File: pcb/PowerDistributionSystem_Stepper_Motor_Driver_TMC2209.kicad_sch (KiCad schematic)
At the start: 19 parts, among them U1 TMC2209-LA-T

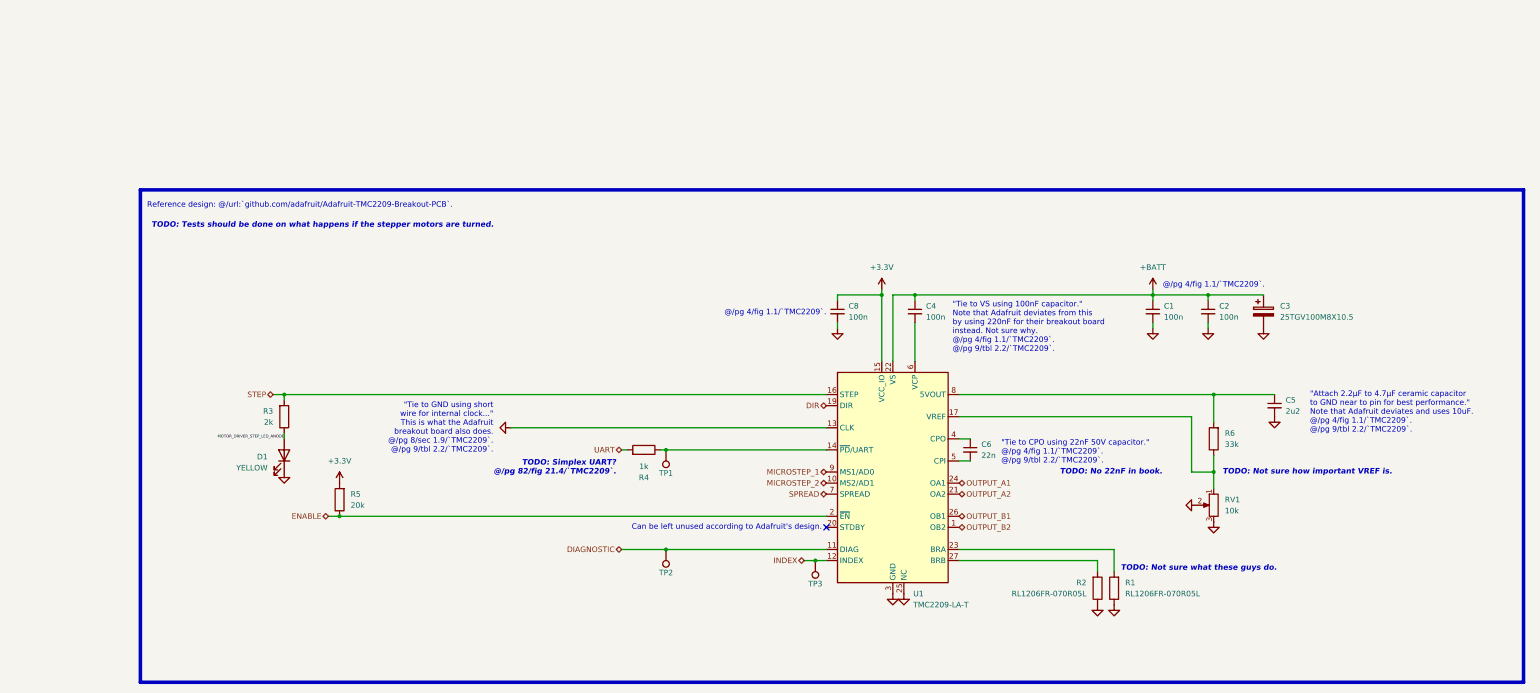
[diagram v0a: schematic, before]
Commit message: Cleaned up small details of the TMC2209.
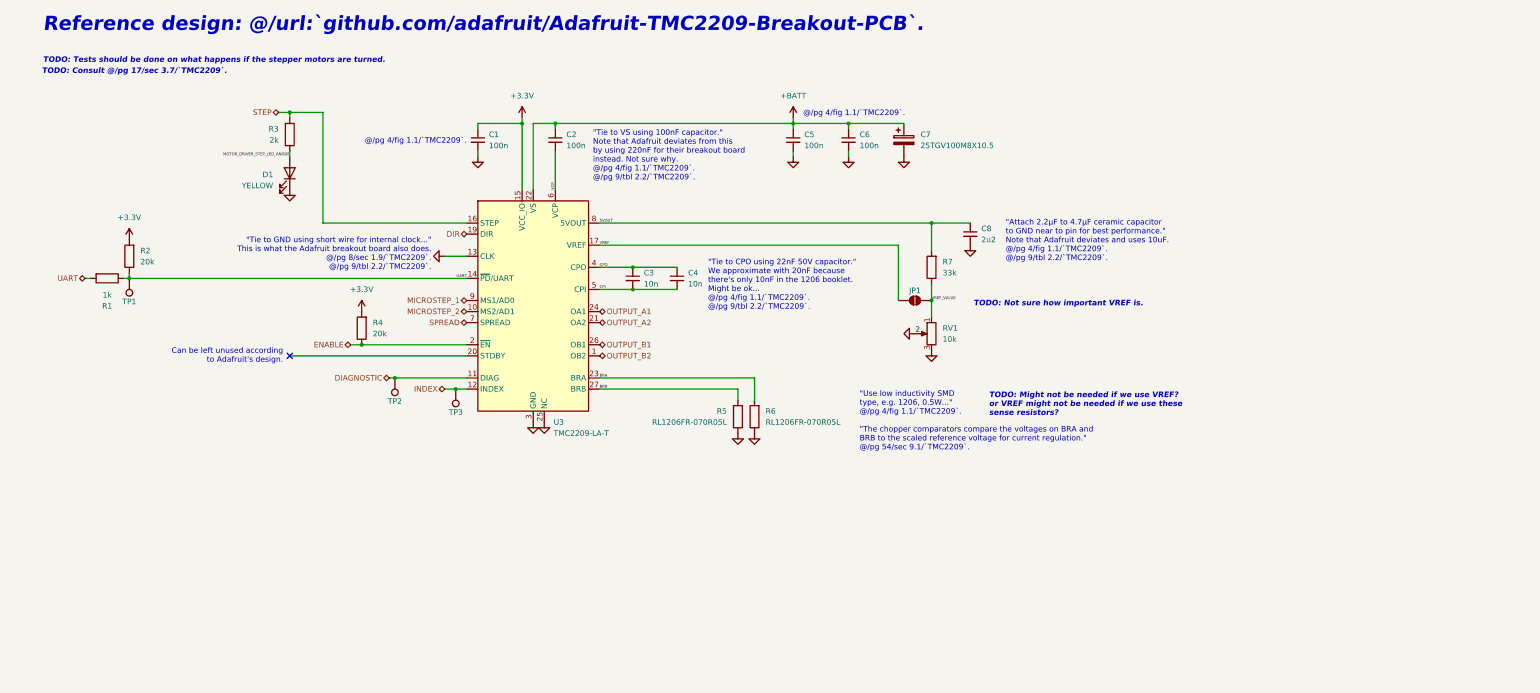
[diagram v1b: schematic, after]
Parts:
- added C4: 10n, Capacitor_SMD:C_1206_3216Metric_Pad1.33x1.80mm_HandSolder, symbol Device:C_Small
- added JP1: SolderJumper_2_Open, symbol Jumper:SolderJumper_2_Open
- added R2: 20k, Resistor_SMD:R_1206_3216Metric_Pad1.30x1.75mm_HandSolder, symbol Device:R
- C3: renamed from C6; value 22n -> 10n
- renumbered C8 to C1, C4 to C2, C1 to C5, C2 to C6, C3 to C7, C5 to C8, R4 to R1, R5 to R4, R2 to R5, R1 to R6, R6 to R7, U1 to U3
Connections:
- net +3.3V: now also R2.2
- net UART: now also R1.1, TP1.1, U3.14 (~{PD}/UART), R2.1
- net CPO: now reaches C3.1, U3.4 (CPO)
- net CPO: now also C4.1
- net CPI: now reaches C3.2, U3.5 (CPI)
- net CPI: now also C4.2
- net BRB: now reaches R5.2, U3.27 (BRB)
- net VREF_VALUE: now reaches R7.1, RV1.1
- net VREF_VALUE: now also JP1.2 (B); no longer U3.17 (VREF)
- net 5VOUT: now reaches C8.1, R7.2, U3.8 (5VOUT)
- net BRA: now reaches R6.2, U3.23 (BRA)
- net VCP: now reaches C2.2, U3.6 (VCP)
- new net VREF: JP1.1 (A), U3.17 (VREF)
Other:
- note added: ""Tie to CPO using 22nF 50V capacitor." We approximate with 20nF because there's only 10nF in the 1206 booklet. Might be ok... @/pg 4/fig 1.1/`TMC2209`. @/pg 9/tbl 2.2/`TMC2209`."
- note added: ""Use low inductivity SMD type, e.g. 1206, 0.5W..." @/pg 4/fig 1.1/`TMC2209`. "The chopper comparators compare the voltages on BRA and BRB to the scaled reference voltage for current regulation." @/pg 54/sec 9.1/`TMC2209`."
- note added: "TODO: Consult @/pg 17/sec 3.7/`TMC2209`."
- note added: "TODO: Might not be needed if we use VREF? or VREF might not be needed if we use these sense resistors?"
- note removed: ""Tie to CPO using 22nF 50V capacitor." @/pg 4/fig 1.1/`TMC2209`. @/pg 9/tbl 2.2/`TMC2209`."
- note removed: "TODO: No 22nF in book."
- note removed: "TODO: Not sure what these guys do."
- note removed: "TODO: Simplex UART? @/pg 82/fig 21.4/`TMC2209`."
- moved on the sheet: C1, C2, C3, C5, C6, C7, C8, D1, R1, R3, R4, R5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

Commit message: Reworked TMC2209 so that the three drivers have things in common (e.g. enable/disable pin).
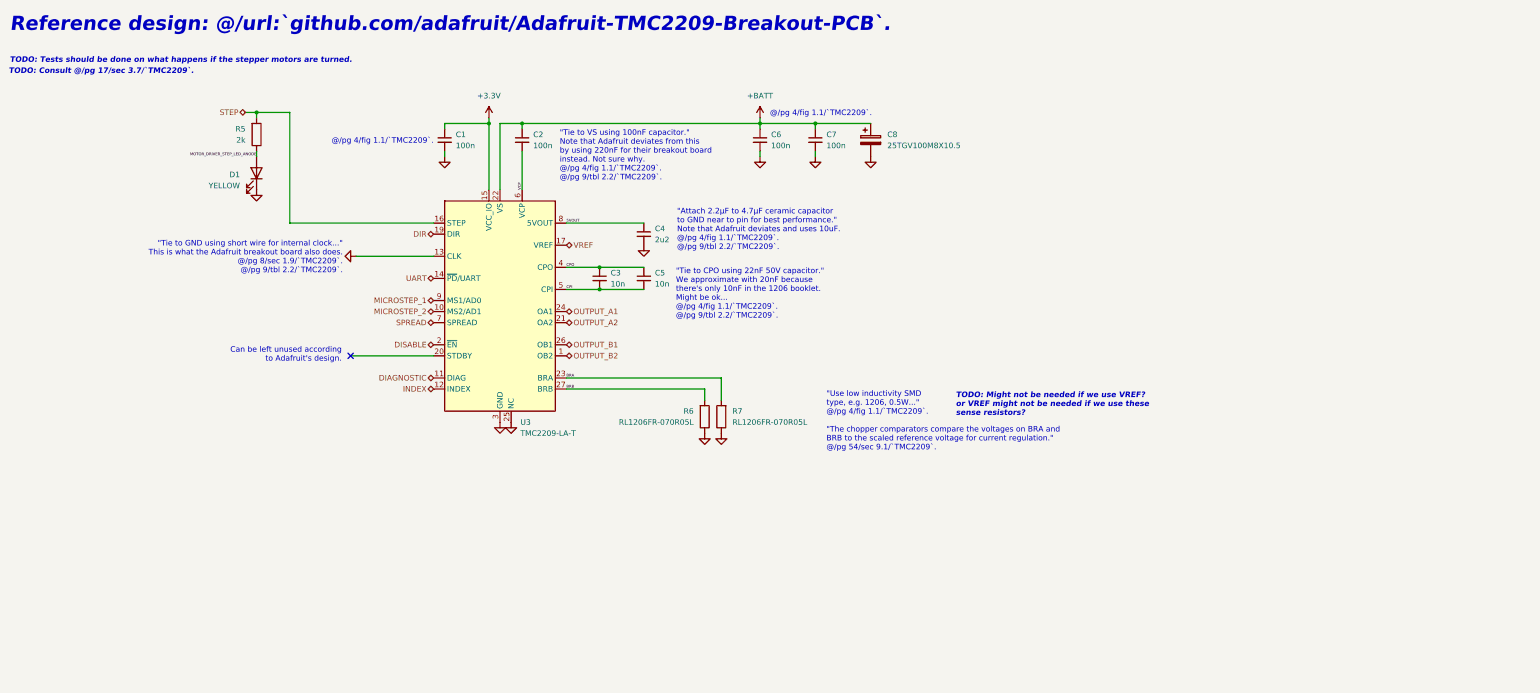
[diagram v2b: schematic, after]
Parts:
- removed JP1: SolderJumper_2_Open, symbol Jumper:SolderJumper_2_Open
- removed R1: 1k, Resistor_SMD:R_1206_3216Metric_Pad1.30x1.75mm_HandSolder, symbol Device:R
- removed R2, R4: 20k, Resistor_SMD:R_1206_3216Metric_Pad1.30x1.75mm_HandSolder, symbol Device:R
- removed R7: 33k, Resistor_SMD:R_1206_3216Metric_Pad1.30x1.75mm_HandSolder, symbol Device:R
- removed RV1: 10k, pcb:TRIM_35WR10KLFTR, symbol Device:R_Potentiometer
- removed TP1, TP2, TP3: TestPoint, TestPoint:TestPoint_Pad_1.0x1.0mm, symbol Connector:TestPoint
- renumbered C8 to C4, C4 to C5, C5 to C6, C6 to C7, C7 to C8, R3 to R5, R5 to R6, R6 to R7
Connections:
- net ENABLE renamed DISABLE
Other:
- note removed: "TODO: Not sure how important VREF is."
- moved on the sheet: C1, C2, C3, C4, C5, C6, C7, C8, D1, R5, R6, R7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

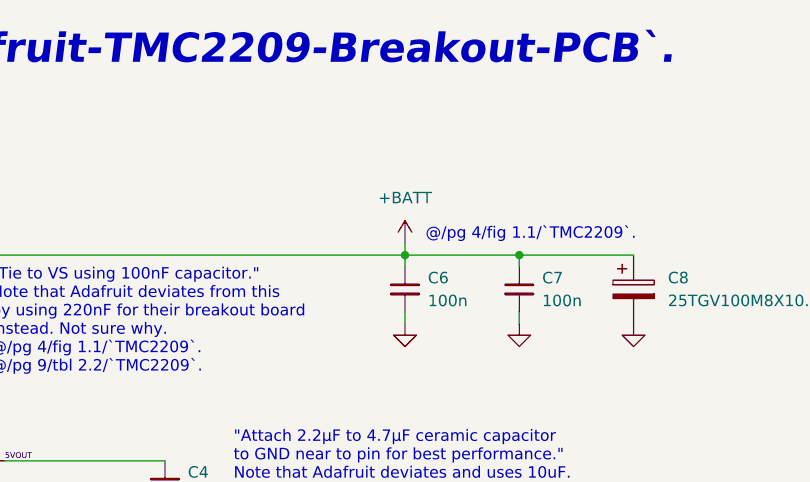
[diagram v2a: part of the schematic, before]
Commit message: Added load switch.
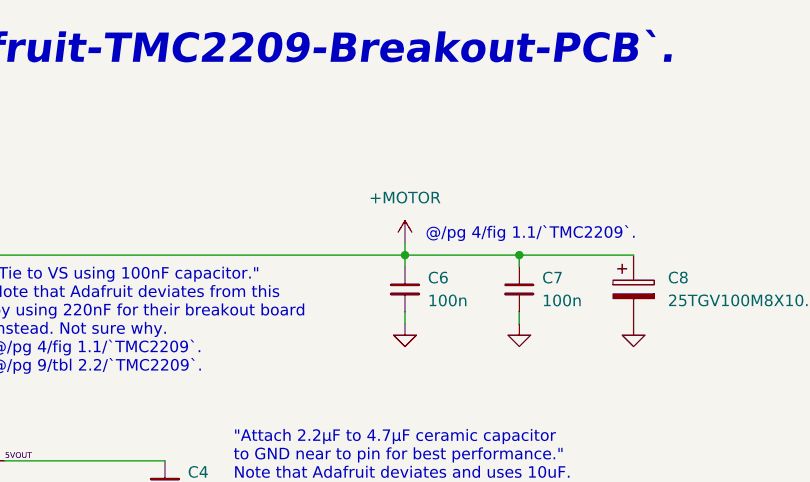
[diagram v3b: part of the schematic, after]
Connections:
- net +BATT renamed +MOTOR
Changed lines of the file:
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@@
 			)
 		)
-		(property "Value" "+BATT"
+		(property "Value" "+MOTOR"
 			(at 189.23 73.66 0)
 			(effects

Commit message: Fixed footprint of TMC2209-LA-T.
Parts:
- U3: footprint Package_DFN_QFN:VQFN-28-1EP_5x5mm_P0.5mm_EP3.7x3.7mm_ThermalVias -> pcb:VQFN-28-1EP_5x5mm_P0.5mm_EP3.7x3.7mm_ThermalVias
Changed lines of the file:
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@@
 			)
 		)
-		(property "Footprint" "Package_DFN_QFN:VQFN-28-1EP_5x5mm_P0.5mm_EP3.7x3.7mm_ThermalVias"
+		(property "Footprint" "pcb:VQFN-28-1EP_5x5mm_P0.5mm_EP3.7x3.7mm_ThermalVias"
 			(at 129.54 151.13 0)
 			(effects

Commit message: Updated power distribution system with new stack-up layout.
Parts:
- U3: footprint pcb:VQFN-28-1EP_5x5mm_P0.5mm_EP3.7x3.7mm_ThermalVias -> Package_DFN_QFN:VQFN-28-1EP_5x5mm_P0.5mm_EP3.7x3.7mm_ThermalVias
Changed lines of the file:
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@@
 			)
 		)
-		(property "Footprint" "pcb:VQFN-28-1EP_5x5mm_P0.5mm_EP3.7x3.7mm_ThermalVias"
+		(property "Footprint" "Package_DFN_QFN:VQFN-28-1EP_5x5mm_P0.5mm_EP3.7x3.7mm_ThermalVias"
 			(at 129.54 151.13 0)
 			(effects

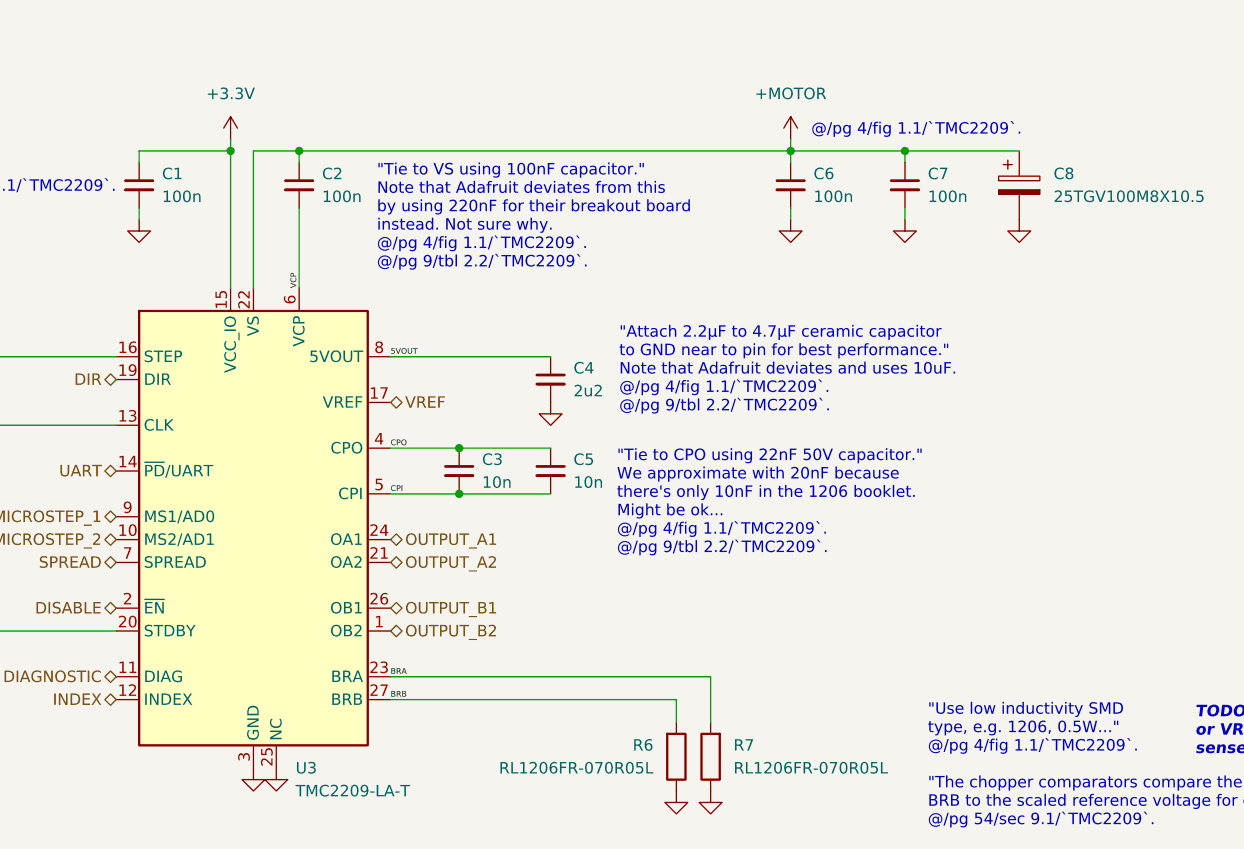
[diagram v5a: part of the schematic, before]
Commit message: Updated `StackConnector` to use reference prefix of "J".
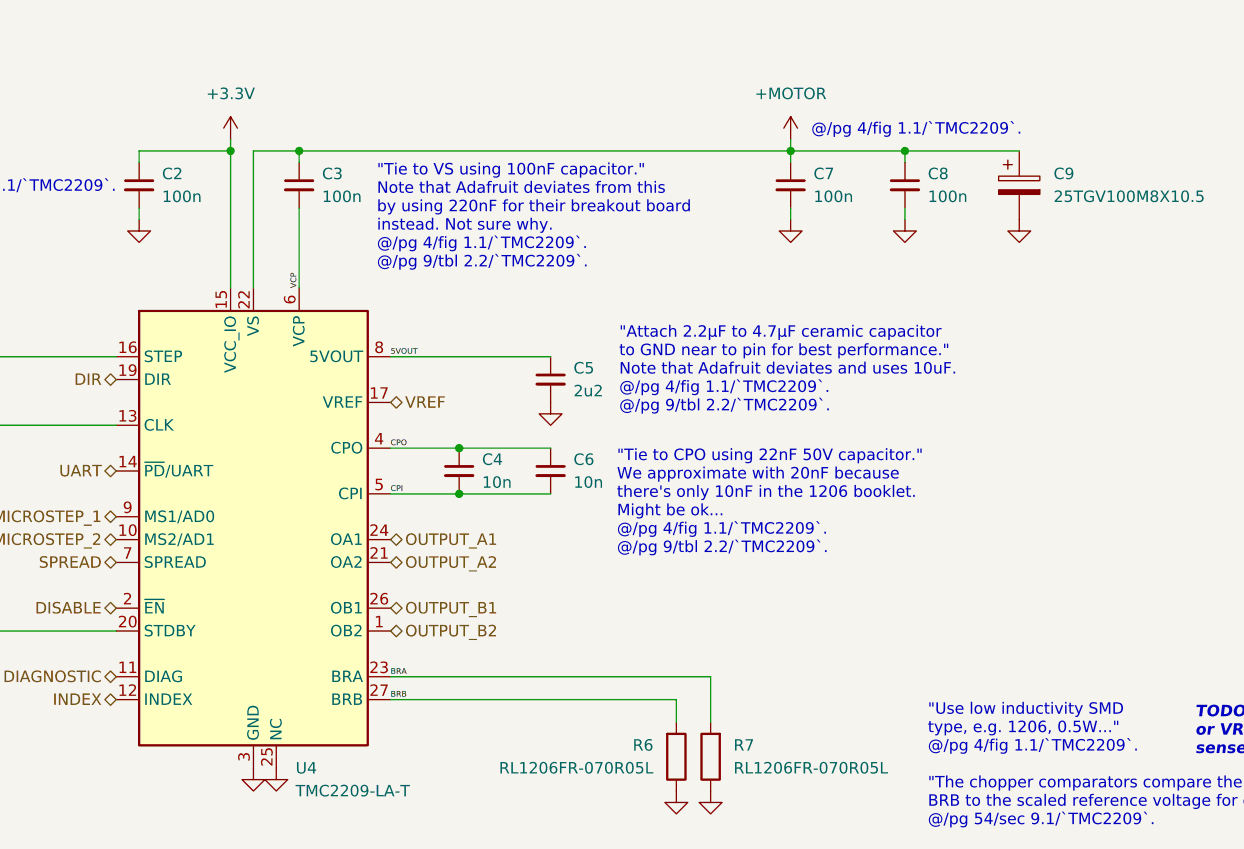
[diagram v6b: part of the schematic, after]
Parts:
- renumbered C1 to C2, C2 to C3, C3 to C4, C4 to C5, C5 to C6, C6 to C7, C7 to C8, C8 to C9, U3 to U4

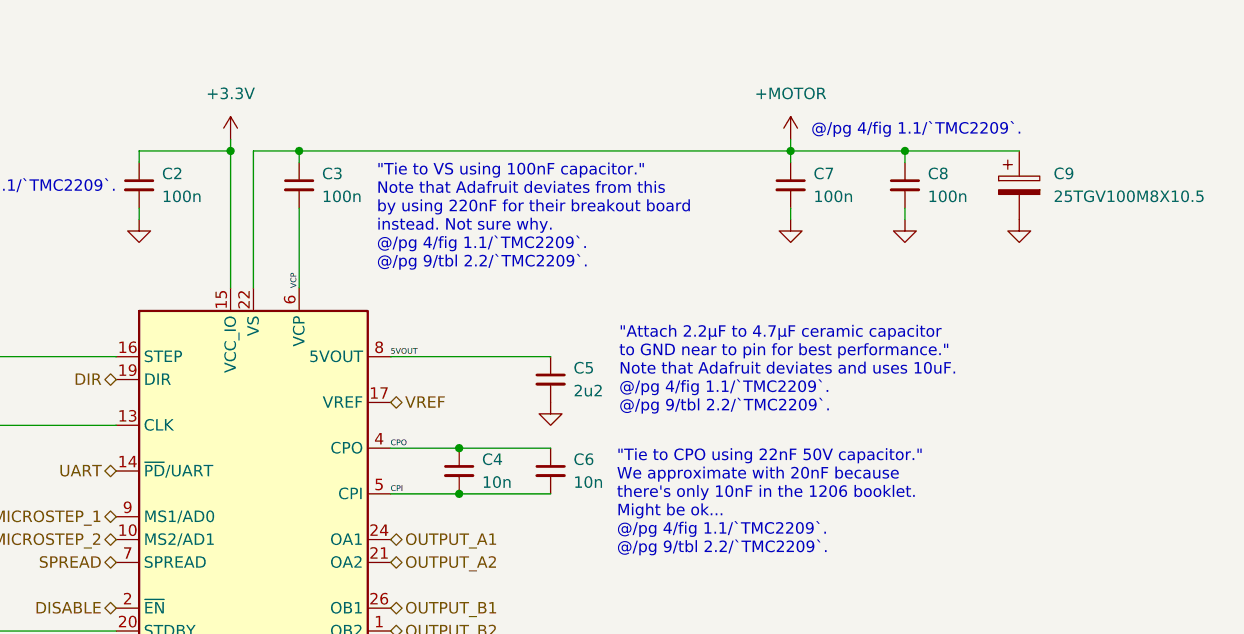
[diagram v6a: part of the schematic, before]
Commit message: Using JST-PA connectors.
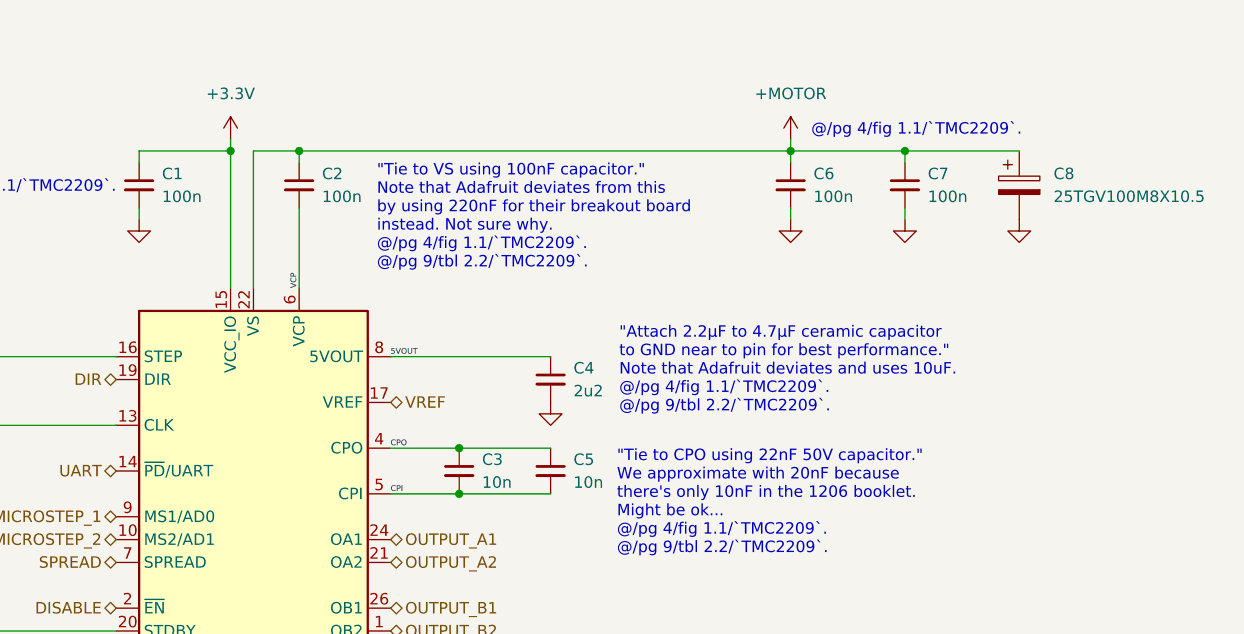
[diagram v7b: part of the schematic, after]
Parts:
- renumbered C2 to C1, C3 to C2, C4 to C3, C5 to C4, C6 to C5, C7 to C6, C8 to C7, C9 to C8
